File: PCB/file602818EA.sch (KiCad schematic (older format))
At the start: 9 parts

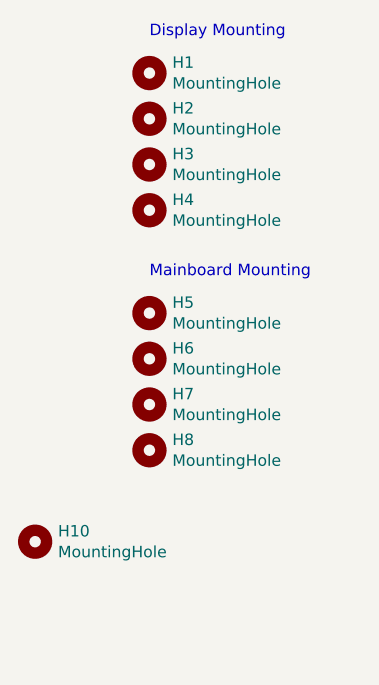
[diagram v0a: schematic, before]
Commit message: Cleaned up repository. Created a BOM in iBOM Format.
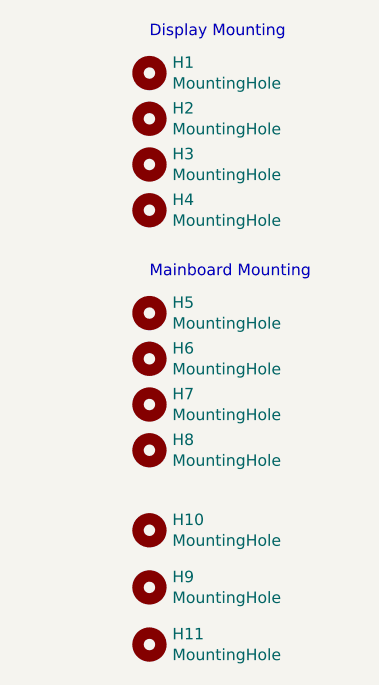
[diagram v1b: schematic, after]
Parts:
- added H11, H9: MountingHole, MountingHole:MountingHole_3.2mm_M3_DIN965_Pad, symbol Mechanical:MountingHole
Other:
- moved on the sheet: H10
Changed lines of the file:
@@
 L Mechanical:MountingHole H10
 U 1 1 601EF31F
-P 850 3250
-F 0 "H10" H 950 3296 50  0000 L CNN
-F 1 "MountingHole" H 950 3205 50  0000 L CNN
-F 2 "MountingHole:MountingHole_3.2mm_M3_DIN965_Pad" H 850 3250 50  0001 C CNN
-F 3 "~" H 850 3250 50  0001 C CNN
-	1    850  3250
+P 1350 3200
+F 0 "H10" H 1450 3246 50  0000 L CNN
+F 1 "MountingHole" H 1450 3155 50  0000 L CNN
+F 2 "MountingHole:MountingHole_3.2mm_M3_DIN965_Pad" H 1350 3200 50  0001 C CNN
+F 3 "~" H 1350 3200 50  0001 C CNN
+	1    1350 3200
 	1    0    0    -1
 $EndComp
@@
 Text Notes 1350 1050 0    50   ~ 0
 Display Mounting
+$Comp
+L Mechanical:MountingHole H9
+U 1 1 60285390
+P 1350 3450
+F 0 "H9" H 1450 3496 50  0000 L CNN
+F 1 "MountingHole" H 1450 3405 50  0000 L CNN
+F 2 "MountingHole:MountingHole_3.2mm_M3_DIN965_Pad" H 1350 3450 50  0001 C CNN
+F 3 "~" H 1350 3450 50  0001 C CNN
+	1    1350 3450
+	1    0    0    -1
+$EndComp
+$Comp
+L Mechanical:MountingHole H11
+U 1 1 6028614A
+P 1350 3700
+F 0 "H11" H 1450 3746 50  0000 L CNN
+F 1 "MountingHole" H 1450 3655 50  0000 L CNN
+F 2 "MountingHole:MountingHole_3.2mm_M3_DIN965_Pad" H 1350 3700 50  0001 C CNN
+F 3 "~" H 1350 3700 50  0001 C CNN
+	1    1350 3700
+	1    0    0    -1
+$EndComp
 $EndSCHEMATC
